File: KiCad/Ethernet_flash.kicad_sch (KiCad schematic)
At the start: 28 parts, among them IC10 MX25UM25645GXDI00-T, IC8 TFP410PAP, IC9 TS3DV642A0RUAR

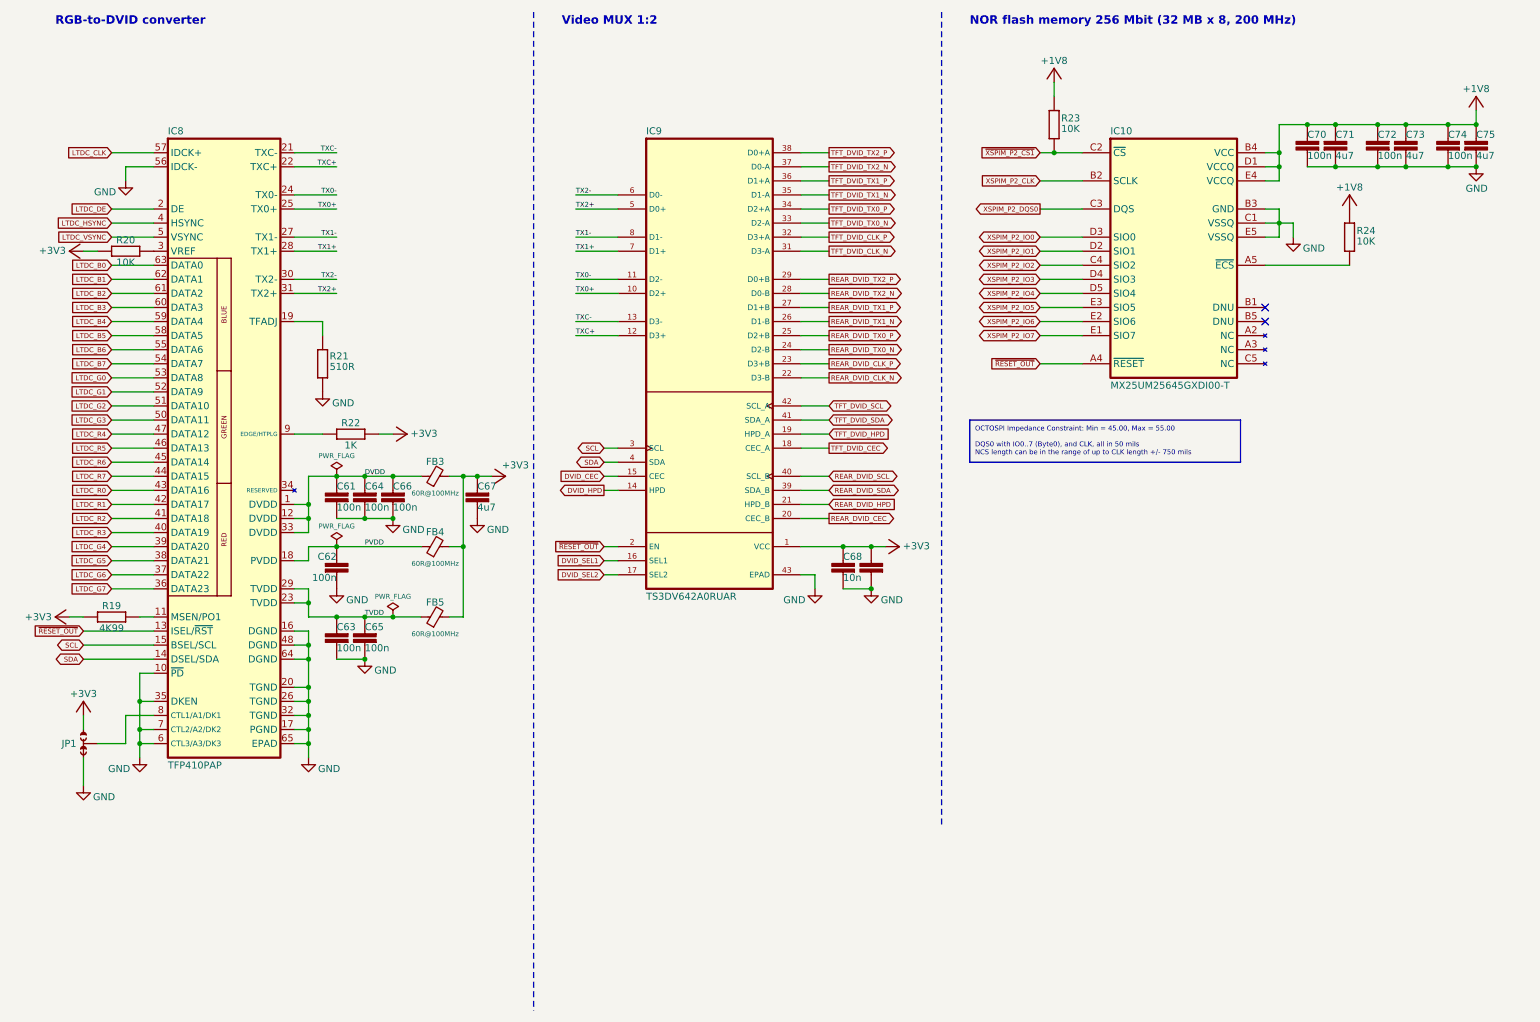
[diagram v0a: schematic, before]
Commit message: BOM update, PCB layout improvements, NetTie positions fixed
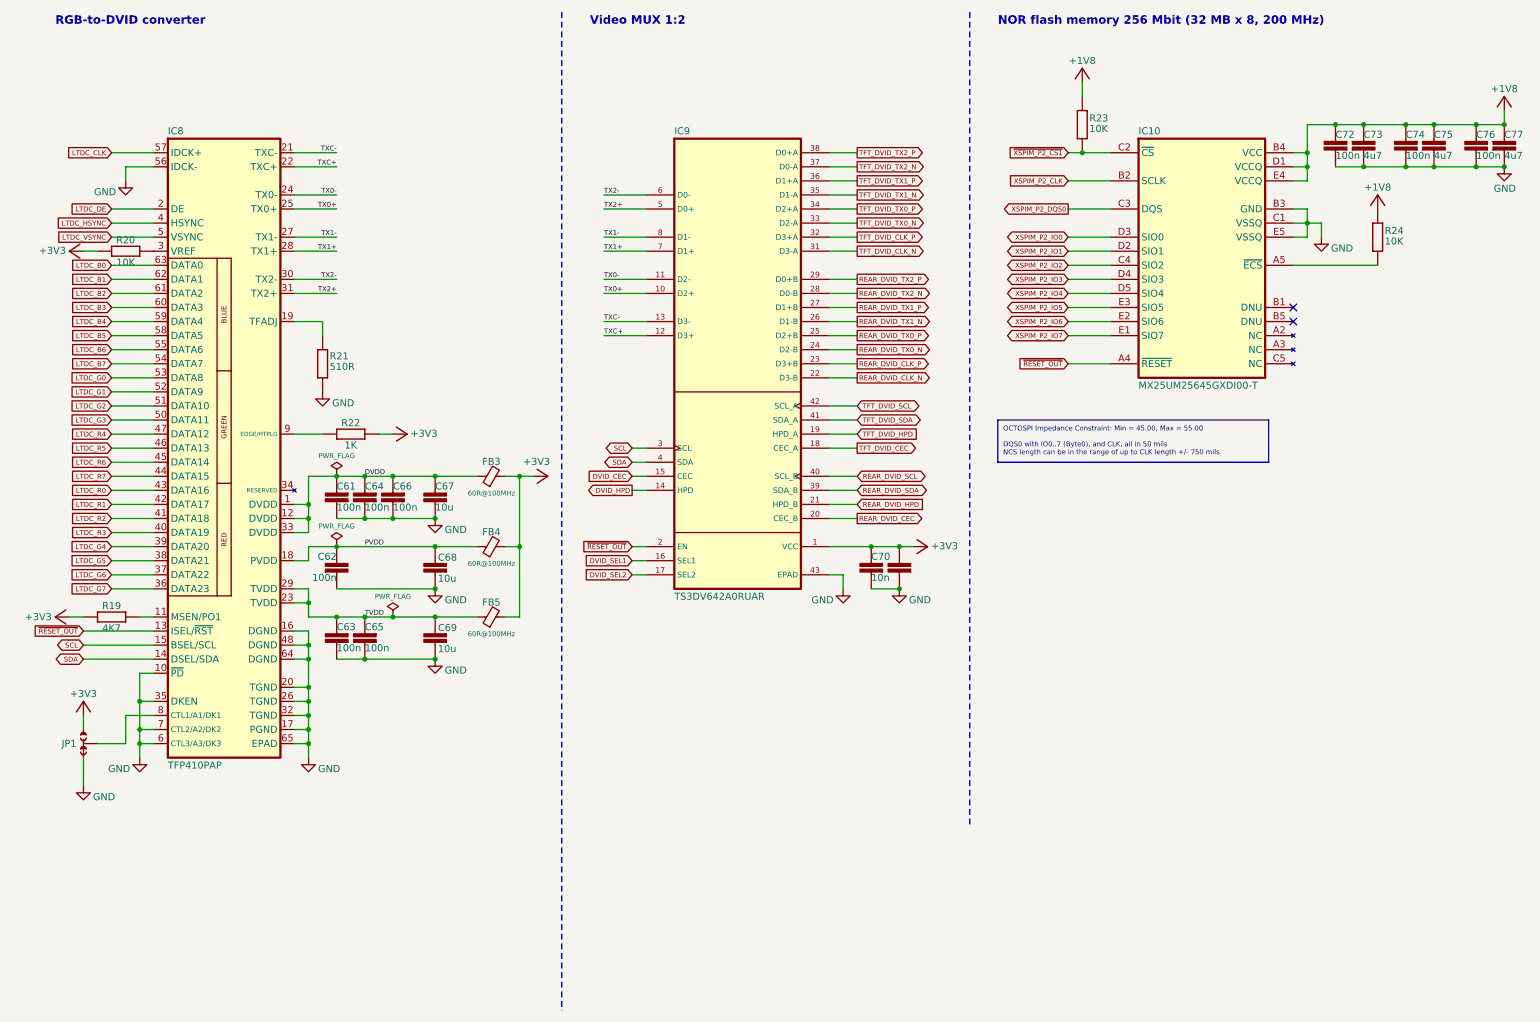
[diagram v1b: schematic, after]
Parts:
- added C68, C69: 10u, PCM_EEZ_passives:C_0603_1608Metric, symbol PCM_EEZ_passives:C-EU
- C67: value 4u7 -> 10u; DigiKey 1276-1044-1-ND -> 1276-1052-6-ND; LCSC C1705 -> C17024; Mouser 187-CL10A475KP8NNND -> 187-CL21A106KPFNNNE; TME CL10A475KP8NNNC -> CL21A106KPFNNNE
- R19: value 4K99 -> 4K7; DigiKey 13-RC0402FR-1349K9LCT-ND -> 13-RC0402FR-104K7LCT-ND; Mouser 603-RC0402FR-1349K9L -> 603-RC0402FR-104K7L; TME SMD0402-49.9K-1% -> SMD0402-4K7-1%
- renumbered C68 to C70, C69 to C71, C70 to C72, C71 to C73, C72 to C74, C73 to C75, C74 to C76, C75 to C77
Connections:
- net +3V3: no longer C67.1
- net DVDD: now also C67.1
- net GND: now also C68.1, C69.1
- net PVDD: now also C68.2
- net TVDD: now also C69.2
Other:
- moved on the sheet: C67, C70, C72, C73, C74, C75, C76, C77, FB3, FB4, FB5, IC10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

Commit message: Removed all blind/burned vias
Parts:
- renumbered R19 to R17, R20 to R18, R21 to R19, R22 to R20, R23 to R21, R24 to R22
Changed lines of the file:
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@@
 		(on_board yes)
 		(dnp no)
-		(property "Reference" "R21"
+		(property "Reference" "R19"
 			(at 67.31 78.105 0)
 			(effects
@@
 			(project "BB3plus CM5 STM32H7 module"
 				(path "/1a4f0aea-3a69-423f-8790-3103cd0321c4/6c545e17-ca5e-4b04-9dff-4169dbe59c9e"
-					(reference "R21")
+					(reference "R19")
 					(unit 1)
 				)
@@
 		(on_board yes)
 		(dnp no)
-		(property "Reference" "R20"
+		(property "Reference" "R18"
 			(at 30.48 57.15 90)
 			(effects
@@
 			(project "BB3plus CM5 STM32H7 module"
 				(path "/1a4f0aea-3a69-423f-8790-3103cd0321c4/6c545e17-ca5e-4b04-9dff-4169dbe59c9e"
-					(reference "R20")
+					(reference "R18")
 					(unit 1)
 				)
@@
 		(on_board yes)
 		(dnp no)
-		(property "Reference" "R22"
+		(property "Reference" "R20"
 			(at 71.12 90.17 90)
 			(effects
@@
 			(project "BB3plus CM5 STM32H7 module"
 				(path "/1a4f0aea-3a69-423f-8790-3103cd0321c4/6c545e17-ca5e-4b04-9dff-4169dbe59c9e"
-					(reference "R22")
+					(reference "R20")
 					(unit 1)
 				)
@@
 		(on_board yes)
 		(dnp no)
-		(property "Reference" "R23"
+		(property "Reference" "R21"
 			(at 204.47 33.655 0)
 			(effects
@@
 			(project "BB3plus CM5 STM32H7 module"
 				(path "/1a4f0aea-3a69-423f-8790-3103cd0321c4/6c545e17-ca5e-4b04-9dff-4169dbe59c9e"
-					(reference "R23")
+					(reference "R21")
 					(unit 1)
 				)
@@
 		(on_board yes)
 		(dnp no)
-		(property "Reference" "R24"
+		(property "Reference" "R22"
 			(at 257.81 53.975 0)
 			(effects
@@
 			(project "BB3plus CM5 STM32H7 module"
 				(path "/1a4f0aea-3a69-423f-8790-3103cd0321c4/6c545e17-ca5e-4b04-9dff-4169dbe59c9e"
-					(reference "R24")
+					(reference "R22")
 					(unit 1)
 				)
@@
 		(on_board yes)
 		(dnp no)
-		(property "Reference" "R19"
+		(property "Reference" "R17"
 			(at 27.94 123.19 90)
 			(effects
@@
 			(project "BB3plus CM5 STM32H7 module"
 				(path "/1a4f0aea-3a69-423f-8790-3103cd0321c4/6c545e17-ca5e-4b04-9dff-4169dbe59c9e"
-					(reference "R19")
+					(reference "R17")
 					(unit 1)
 				)
